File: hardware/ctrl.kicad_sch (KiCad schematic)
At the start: 22 parts, among them J1 USB_C_Receptacle_USB2.0_16P, SW2 SW_Push, U1 ESP32-C3-WROOM-02

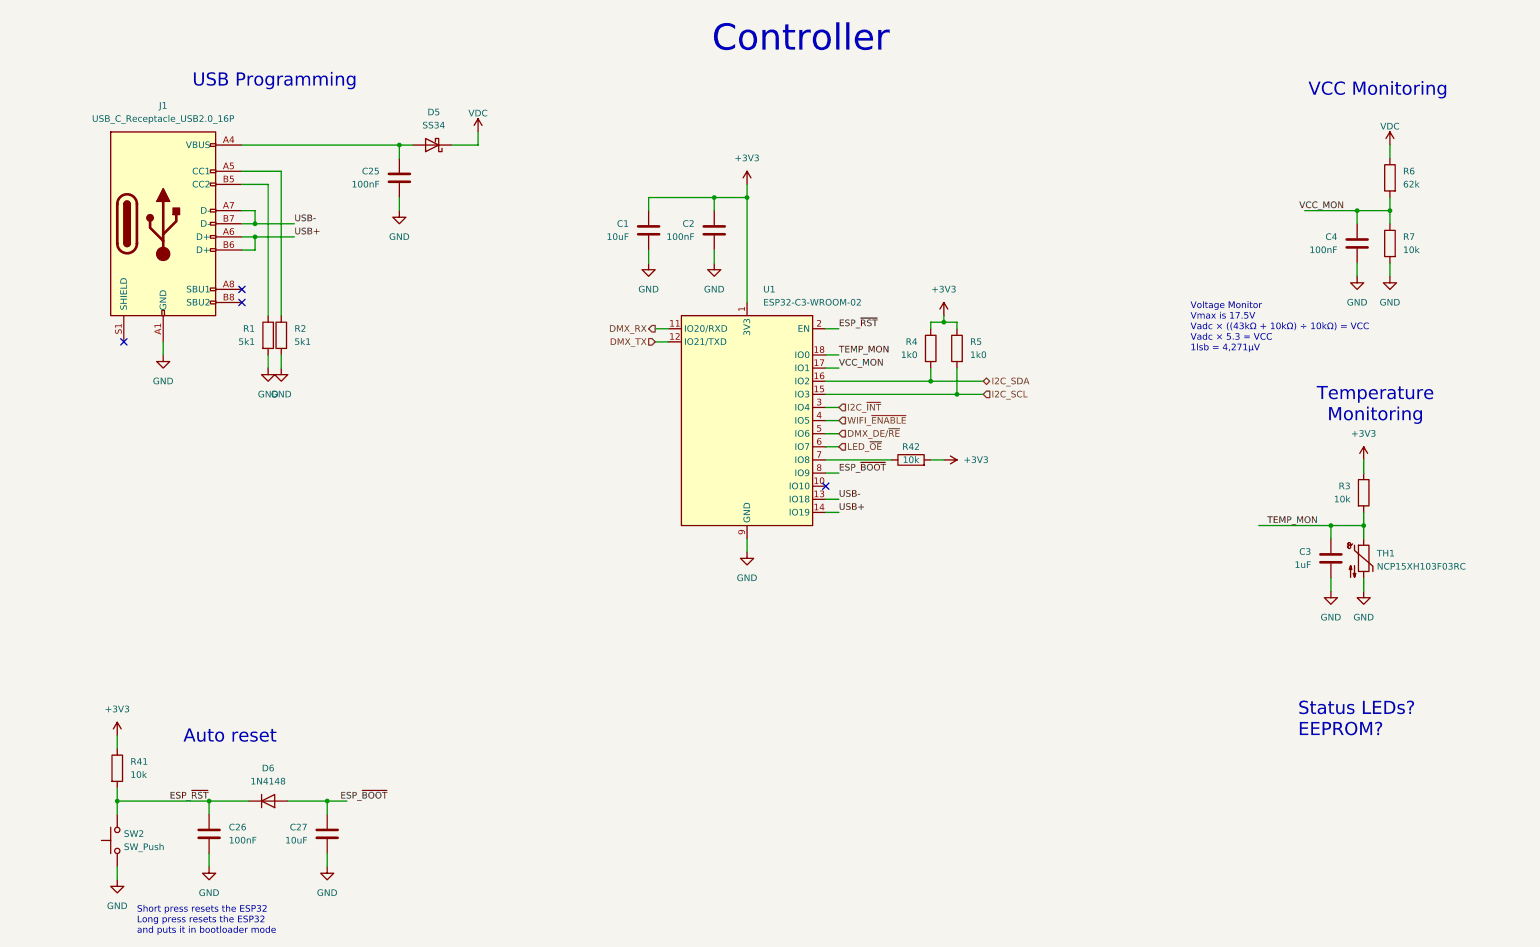
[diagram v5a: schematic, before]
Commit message: updating PSUs
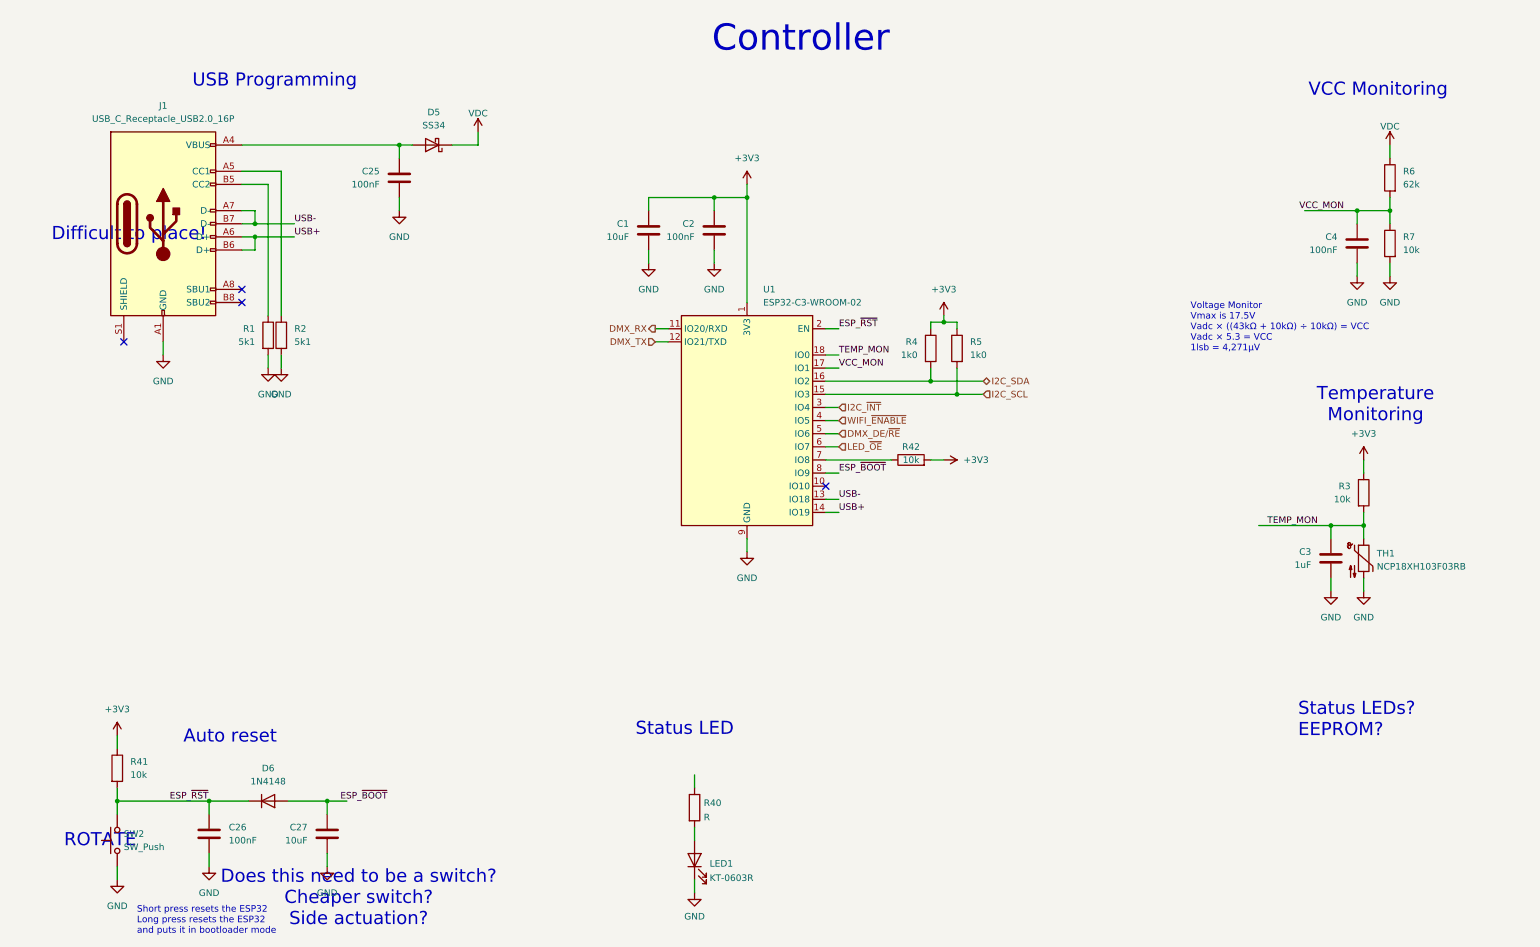
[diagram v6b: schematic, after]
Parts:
- added LED1: KT-0603R, LED_SMD:LED_0603_1608Metric, symbol Device:LED
- added R40: R, Resistor_SMD:R_0603_1608Metric, symbol Device:R
- C1, C27: LCSC (none) -> C15850
- C2, C25, C26, C4: LCSC (none) -> C14663
- C3: LCSC (none) -> C15849
- D6: footprint (none) -> Diode_SMD:D_SOD-123
- R1, R2: LCSC (none) -> C23186
- R3, R4, R41, R42, R5, R7: LCSC (none) -> C21190
- R6: LCSC (none) -> C23221
- SW2: LCSC (none) -> C231329
- TH1: value NCP15XH103F03RC -> NCP18XH103F03RB; LCSC C77131 -> C13564; MPN NCP15XH103F03RC -> NCP18XH103F03RB
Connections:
- net GND: now also LED1.1 (K)
- new net: LED1.2 (A), R40.2
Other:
- note added: "Difficult to place!"
- note added: "Does this need to be a switch? Cheaper switch? Side actuation?"
- note added: "ROTATE"
- note added: "Status LED"

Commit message: some jlc cleanup
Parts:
- D6: value 1N4148 -> BAT54WS; footprint Diode_SMD:D_SOD-123 -> Diode_SMD:D_SOD-323; LCSC (none) -> C7502694
- R3, R41, R42, R7: LCSC C21190 -> C25804
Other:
- note added: "Difficult to place! Missing 3D model"
- note added: "Status LEDs?"
- note removed: "Difficult to place!"
- note removed: "Status LEDs? EEPROM?"
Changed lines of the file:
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@@
 		(company "Wires & Bits")
 	)
-	(text "Difficult to place!"
+	(text "Difficult to place!\nMissing 3D model"
 		(exclude_from_sim no)
 		(at 23.876 56.642 0)
@@
 		)
 	)
-	(text "Status LEDs?\nEEPROM?"
+	(text "Status LEDs?"
 		(exclude_from_sim no)
-		(at 250.19 150.622 0)
+		(at 134.62 156.21 0)
 		(effects
 			(font
@@
 	(text "Does this need to be a switch?\nCheaper switch?\nSide actuation?"
 		(exclude_from_sim no)
-		(at 68.326 185.166 0)
+		(at 91.694 160.782 0)
 		(effects
 			(font
@@
 			)
 		)
-		(property "LCSC" "C21190"
+		(property "LCSC" "C25804"
 			(at 21.59 160.02 0)
 			(effects
@@
 			)
 		)
-		(property "LCSC" "C21190"
+		(property "LCSC" "C25804"
 			(at 267.97 58.42 0)
 			(effects
@@
 			)
 		)
-		(property "LCSC" "C21190"
+		(property "LCSC" "C25804"
 			(at 262.89 106.68 0)
 			(effects
@@
 			)
 		)
-		(property "LCSC" "C21190"
+		(property "LCSC" "C25804"
 			(at 175.26 100.33 90)
 			(effects
@@
 			)
 		)
-		(property "Value" "1N4148"
+		(property "Value" "BAT54WS"
 			(at 50.8 162.56 0)
 			(effects
@@
 			)
 		)
-		(property "Footprint" "Diode_SMD:D_SOD-123"
+		(property "Footprint" "Diode_SMD:D_SOD-323"
 			(at 50.8 166.37 0)
 			(effects
@@
 			(at 50.8 166.37 0)
 			(effects
+				(font
+					(size 1.27 1.27)
+				)
+				(hide yes)
+			)
+		)
+		(property "LCSC" "C7502694"
+			(at 50.8 166.37 0)
+			(effects

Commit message: tweaking lcsc part numbers
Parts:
- C1, C27: value 10uF -> 10uF 25V
- C3: value 1uF -> 1uF 50V
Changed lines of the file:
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@@
 			)
 		)
-		(property "Value" "10uF"
+		(property "Value" "10uF 25V"
 			(at 58.42 173.9899 0)
 			(effects
@@
 			)
 		)
-		(property "Value" "1uF"
+		(property "Value" "1uF 50V"
 			(at 252.73 120.6499 0)
 			(effects
@@
 			)
 		)
-		(property "Value" "10uF"
+		(property "Value" "10uF 25V"
 			(at 120.65 57.1499 0)
 			(effects
